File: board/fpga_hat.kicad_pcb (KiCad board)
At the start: 2 copper layers, 65 x 56.5 mm, 4 parts

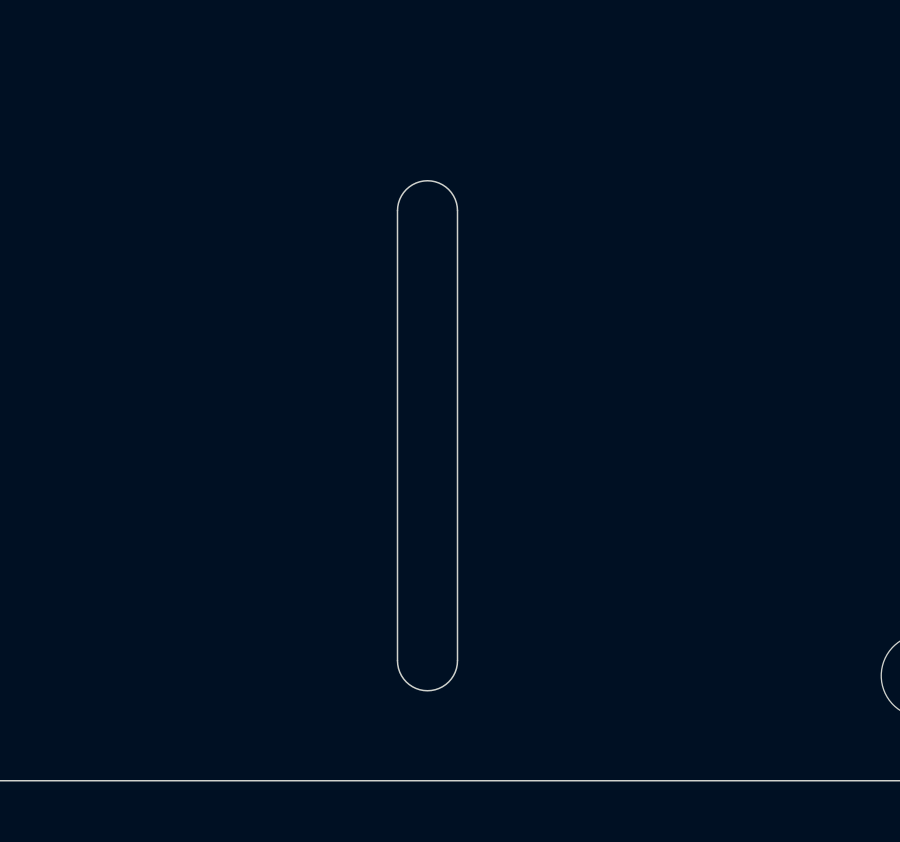
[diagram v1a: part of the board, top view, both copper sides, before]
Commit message: Add 5V header to schematic -- useful for some PMODs. Move camera slot 1.5mm to right, to leave room for PMODs.
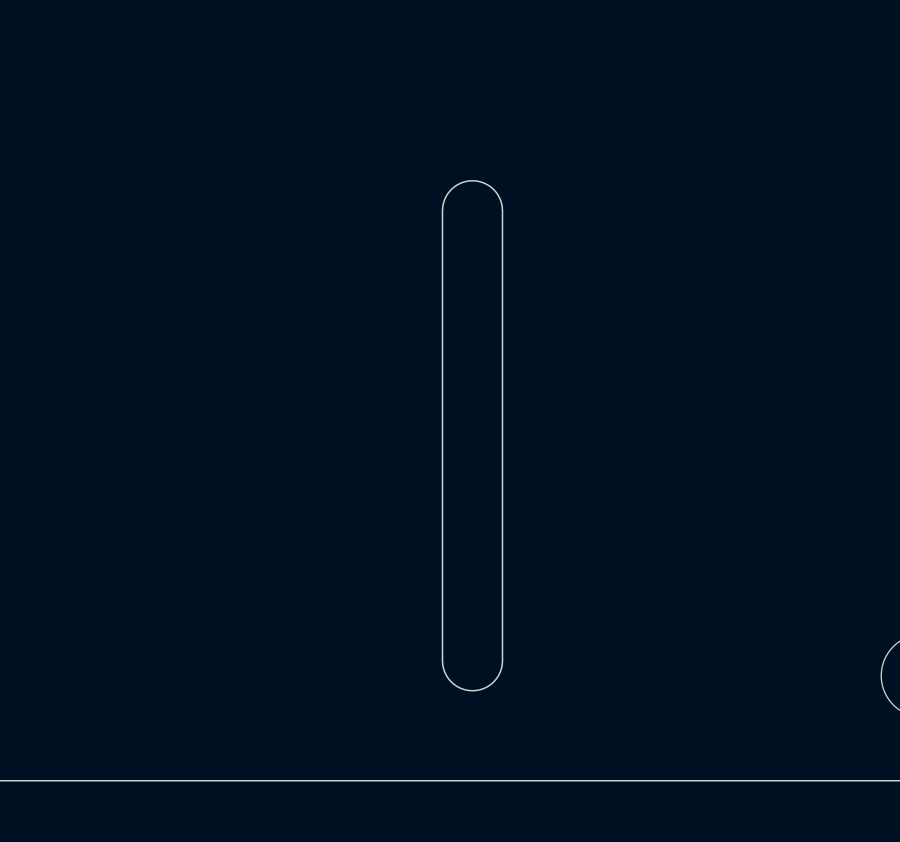
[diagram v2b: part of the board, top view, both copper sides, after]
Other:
- outline, holes or cut-outs redrawn
- net class Default: clearance 0.2 -> 0.09; trace_width 0.25 -> 0.09; via_dia 0.8 -> 0.45; via_drill 0.4 -> 0.2
- rule trace_clearance: 0.2 -> 0.09
- rule trace_min: 0.2 -> 0.09
- rule via_min_drill: 0.3 -> 0.2
- rule via_min_size: 0.4 -> 0.45
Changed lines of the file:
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@@
   )
   (setup
-    (last_trace_width 0.25)
-    (trace_clearance 0.2)
+    (last_trace_width 0.09)
+    (user_trace_width 0.15)
+    (user_trace_width 0.25)
+    (user_trace_width 0.5)
+    (trace_clearance 0.09)
     (zone_clearance 0.508)
     (zone_45_only no)
-    (trace_min 0.2)
-    (via_size 0.8)
-    (via_drill 0.4)
-    (via_min_size 0.4)
-    (via_min_drill 0.3)
+    (trace_min 0.09)
+    (via_size 0.45)
+    (via_drill 0.2)
+    (via_min_size 0.45)
+    (via_min_drill 0.2)
     (uvia_size 0.3)
     (uvia_drill 0.1)
@@
   (net 0 "")
   (net_class Default "This is the default net class."
-    (clearance 0.2)
-    (trace_width 0.25)
-    (via_dia 0.8)
-    (via_drill 0.4)
+    (clearance 0.09)
+    (trace_width 0.09)
+    (via_dia 0.45)
+    (via_drill 0.2)
     (uvia_dia 0.3)
     (uvia_drill 0.1)
@@
       (solder_mask_margin 1.725) (zone_connect 0) (thermal_gap 1.9))
   )
-  (gr_line (start 144 117.5) (end 144 132.5) (layer Edge.Cuts) (width 0.05))
-  (gr_line (start 146 132.5) (end 146 117.5) (layer Edge.Cuts) (width 0.05))
-  (gr_arc (start 145 117.5) (end 146 117.5) (angle -180) (layer Edge.Cuts) (width 0.05))
-  (gr_arc (start 145 132.5) (end 144 132.5) (angle -180) (layer Edge.Cuts) (width 0.05))
+  (gr_arc (start 101 118) (end 101 117) (angle -90) (layer Edge.Cuts) (width 0.05))
+  (gr_line (start 101 100) (end 104 100) (layer Edge.Cuts) (width 0.05))
+  (gr_line (start 105 101) (end 105 116) (layer Edge.Cuts) (width 0.05))
+  (gr_line (start 101 117) (end 104 117) (layer Edge.Cuts) (width 0.05))
+  (gr_arc (start 104 101) (end 105 101) (angle -90) (layer Edge.Cuts) (width 0.05))
+  (gr_arc (start 104 116) (end 104 117) (angle -90) (layer Edge.Cuts) (width 0.05))
+  (gr_arc (start 101 99) (end 100 99) (angle -90) (layer Edge.Cuts) (width 0.05))
+  (gr_line (start 165 83) (end 165 133.5) (layer Edge.Cuts) (width 0.05))
+  (gr_line (start 145.5 117.5) (end 145.5 132.5) (layer Edge.Cuts) (width 0.05))
+  (gr_line (start 147.5 132.5) (end 147.5 117.5) (layer Edge.Cuts) (width 0.05))
+  (gr_arc (start 146.5 117.5) (end 147.5 117.5) (angle -180) (layer Edge.Cuts) (width 0.05))
+  (gr_arc (start 146.5 132.5) (end 145.5 132.5) (angle -180) (layer Edge.Cuts) (width 0.05))
   (gr_line (start 100 99) (end 100 83) (layer Edge.Cuts) (width 0.05))
   (gr_line (start 100 133.5) (end 100 118) (layer Edge.Cuts) (width 0.05))
-  (gr_line (start 101 117) (end 104 117) (layer Edge.Cuts) (width 0.05))
-  (gr_line (start 101 100) (end 104 100) (layer Edge.Cuts) (width 0.05))
-  (gr_arc (start 101 99) (end 100 99) (angle -90) (layer Edge.Cuts) (width 0.05))
-  (gr_arc (start 101 118) (end 101 117) (angle -90) (layer Edge.Cuts) (width 0.05))
-  (gr_arc (start 104 116) (end 104 117) (angle -90) (layer Edge.Cuts) (width 0.05))
-  (gr_arc (start 104 101) (end 105 101) (angle -90) (layer Edge.Cuts) (width 0.05))
-  (gr_line (start 105 101) (end 105 116) (layer Edge.Cuts) (width 0.05))
   (gr_arc (start 162 83) (end 165 83) (angle -90) (layer Edge.Cuts) (width 0.05))
   (gr_arc (start 162 133.5) (end 162 136.5) (angle -90) (layer Edge.Cuts) (width 0.05))
@@
   (gr_arc (start 103 83) (end 103 80) (angle -90) (layer Edge.Cuts) (width 0.05))
   (gr_line (start 162 136.5) (end 103 136.5) (layer Edge.Cuts) (width 0.05))
-  (gr_line (start 165 83) (end 165 133.5) (layer Edge.Cuts) (width 0.05))
   (gr_line (start 103 80) (end 162 80) (layer Edge.Cuts) (width 0.05))
 )
